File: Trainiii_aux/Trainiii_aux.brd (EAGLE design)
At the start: 33 x 82 mm, 21 parts, among them J1 ULTRASONIC_OUT, J10 ULTRASONIC_IN, J2 LINE_SENSOR_1_OUT, J3 LINE_SENSOR_2_OUT, J4 ENCODER_1_OUT, J5 ENCODER_2_OUT, J6 ENCODER_1_IN, J7 ENCODER_2_IN, J8 PWR_IN, J9 ANALOG_IN, Q1 BSS138

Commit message: Finish initial version of Aux board
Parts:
- added U$2: (no value), RoboJackets-Aesthetics:ROBOJACKETS
- added U$3: (no value), RoboJackets-Aesthetics:ROBOBUZZ_0.8X
- moved Q1 7.28 mm to (13.2, 39.5)
- moved R1 5.39 mm to (18.0, 43.0), turned to 90 degrees
- moved J10 5.00 mm to (23.0, 37.0)
- moved J6 5.00 mm to (23.0, 54.0)
- moved J7 5.00 mm to (23.0, 66.0)
- moved J8 5.00 mm to (23.0, 25.0)
- moved J9 5.00 mm to (23.0, 8.00)
- moved R4 5.00 mm to (14.0, 47.0)
- moved R2 4.24 mm to (10.0, 40.0)
- moved R3 4.00 mm to (10.0, 47.0)
- moved R5 3.01 mm to (10.0, 58.2)
- moved R6 3.01 mm to (10.0, 70.2)
- moved J2 1.00 mm to (5.00, 9.00)
- moved R7 1.00 mm to (15.0, 32.0)
- moved R8 1.00 mm to (15.0, 28.0)
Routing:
- net GND: track 210.0 -> 4.77 mm, vias 0 -> 3
- net +3V3: track 0.00 -> 148.6 mm
- net +5V: track 0.00 -> 78.7 mm
- net LINE_1_ANALOG: track 0.00 -> 19.7 mm
- net LINE_2_ANALOG: track 0.00 -> 19.0 mm
- net ENCODER_2_TICK: track 0.00 -> 18.0 mm
- net ENCODER_1_TICK: track 0.00 -> 18.0 mm
- net ECHO_3V3: track 0.00 -> 14.3 mm
- net TRIG_3V3: track 0.00 -> 11.0 mm
- net TRIG_5V: track 0.00 -> 8.17 mm
- net ECHO_5V: track 0.00 -> 5.86 mm
- net 5V_LED: track 0.00 -> 4.87 mm
- net 3V3_LED: track 0.00 -> 4.87 mm
- added copper zone on layer 16, net GND
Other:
- board size 33 x 82 mm -> 28 x 82 mm
- board text added: "ADC"
- board text added: "E1"
- board text added: "E3"
- board text added: "ENCODER 1"
- board text added: "ENCODER 2"
- board text added: "GP0"
- board text added: "LINE 1"
- board text added: "LINE 2"
- board text added: "PWR"
- board text added: "Trainiii Auxilary Sensor Board August 2019 v1.0"
- board text added: "ULTRASONIC"

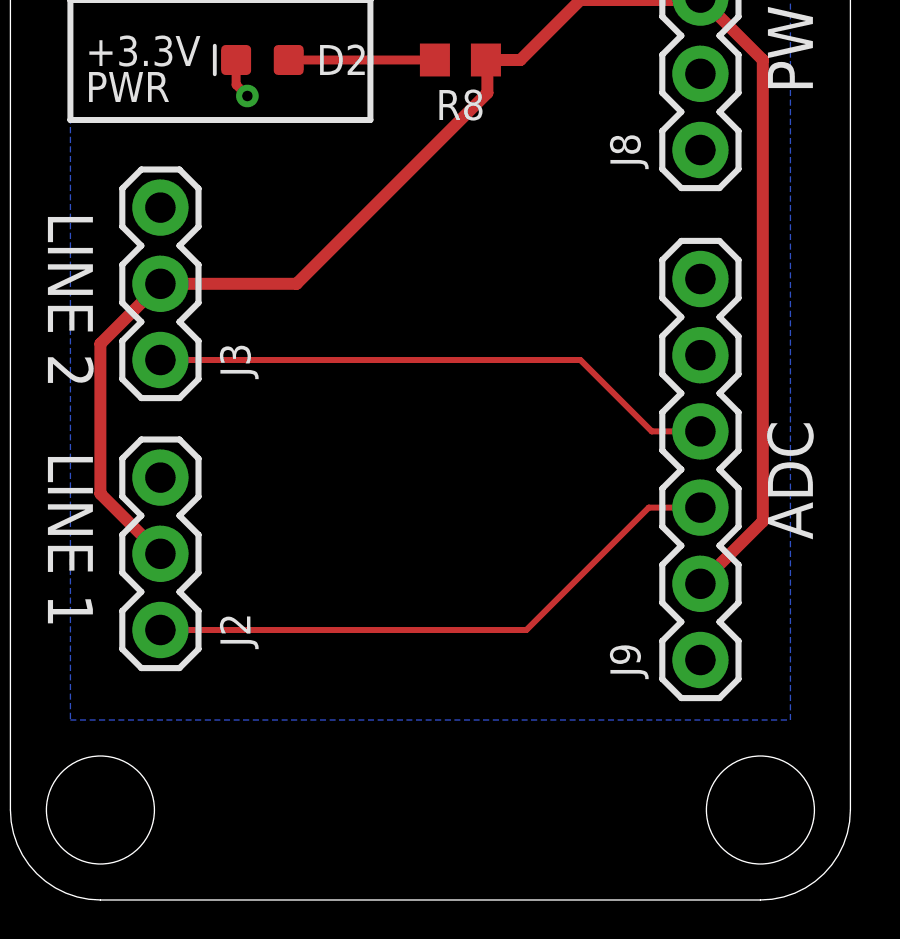
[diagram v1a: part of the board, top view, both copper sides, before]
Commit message: Flipped location of RoboJackets, RoboBuzz
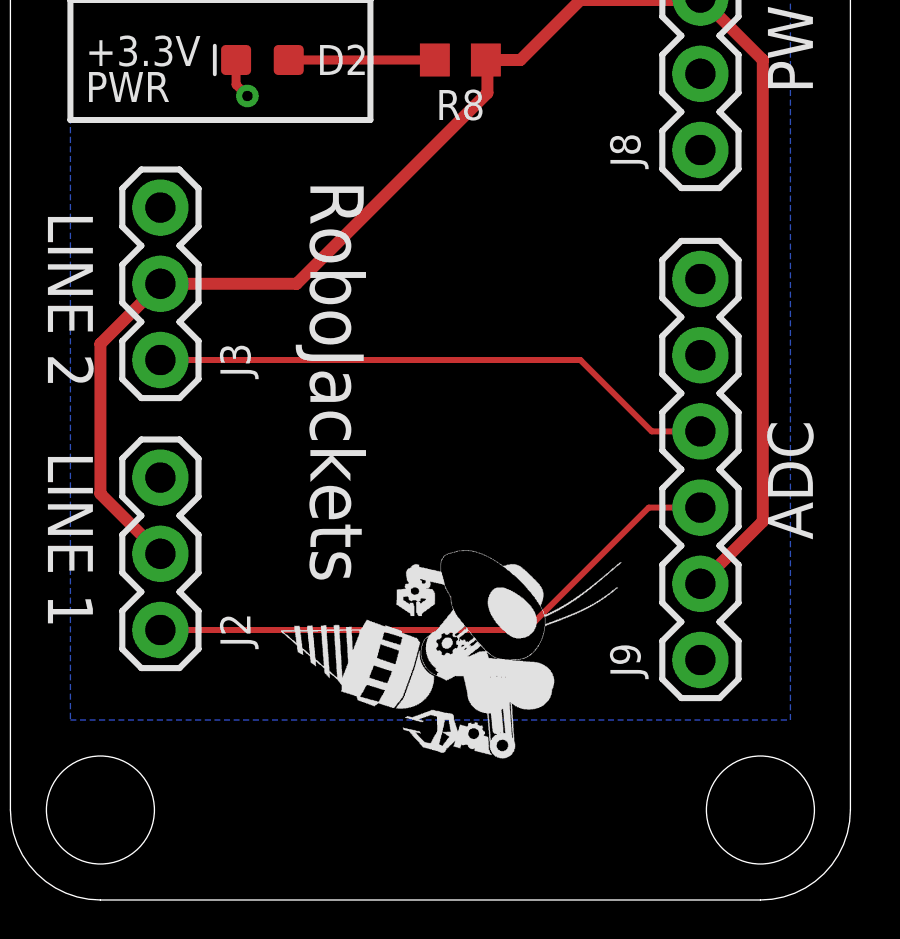
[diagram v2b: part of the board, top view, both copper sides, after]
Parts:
- removed U$2: (no value), RoboJackets-Aesthetics:ROBOJACKETS
- removed U$3: (no value), RoboJackets-Aesthetics:ROBOBUZZ_0.8X
- added U$1: (no value), RoboJackets-Aesthetics:ROBOBUZZ_0.6X
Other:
- board text added: "RoboJackets"
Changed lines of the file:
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@@
 <vertex x="8" y="43"/>
 </polygon>
+<text x="10" y="24" size="1.778" layer="21" font="vector" ratio="13" rot="SR270">RoboJackets</text>
 </plain>
 <attributes>
@@
 <attribute name="VENDOR" value="Fairchild Semiconductor" x="17" y="56" size="1.778" layer="27" rot="R90" display="off"/>
 </element>
-<element name="U$2" library="RoboJackets-Aesthetics" package="ROBOJACKETS" value="" x="9" y="13" smashed="yes" rot="MR90"/>
-<element name="U$3" library="RoboJackets-Aesthetics" package="ROBOBUZZ_0.8X" value="" x="6" y="6" smashed="yes" rot="MR90"/>
+<element name="U$1" library="RoboJackets-Aesthetics" package="ROBOBUZZ_0.6X" value="" x="9" y="9" smashed="yes" rot="R270"/>
 </elements>
 <signals>
